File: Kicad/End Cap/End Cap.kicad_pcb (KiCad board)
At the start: 2 copper layers, 45 x 5 mm, 12 parts, among them J1 1.27mm 4 pin header, J2 Keystone 3579, J3 Keystone 3569, J4 Keystone 3579, J5 Keystone 3569, J6 Keystone 3579, J7 Keystone 3569, J8 Keystone 3579, J9 Keystone 3569

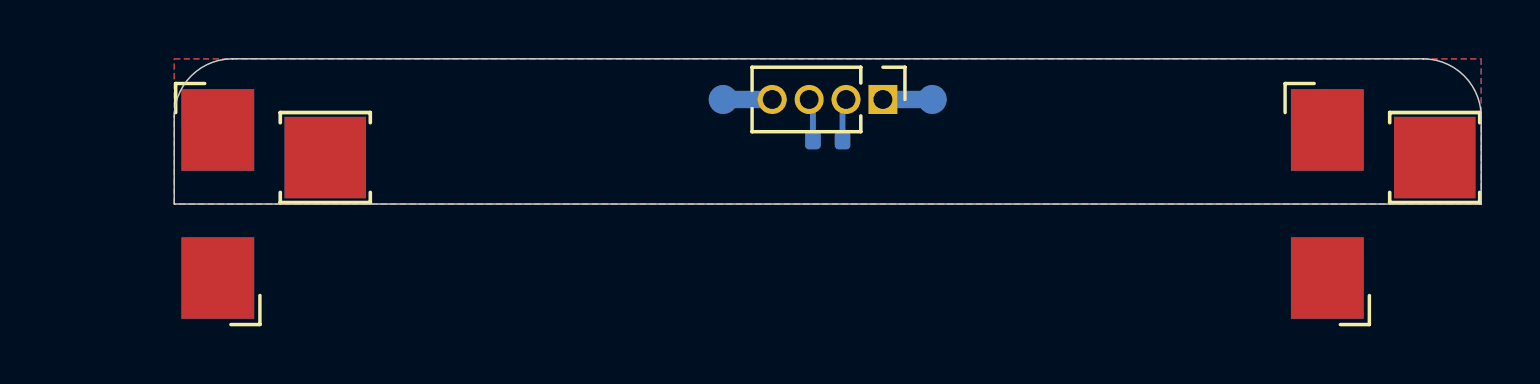
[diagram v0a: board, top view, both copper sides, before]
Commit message: Exported 3D model for End Cap
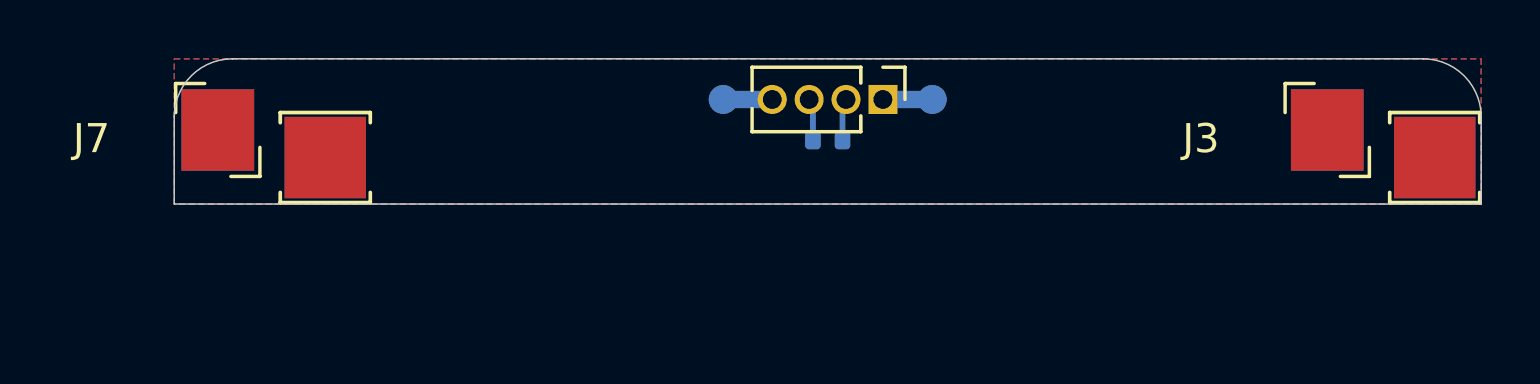
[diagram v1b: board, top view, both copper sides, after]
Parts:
- J3, J5, J7, J9: footprint custom_Connector:Keystone_3569 -> custom_Connector:Keystone_3569_half
- turned J3 to 180 degrees
- turned J5 to 0 degrees
- turned J7 to 180 degrees
- turned J9 to 0 degrees

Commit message: Fixed headers and connectors miss-alignments
Almost everything was misaligned. The holes on the hub to hub headers must be 2.9mm from the edge, the header holes on the motor drivers must be 4.5mm from the edge, and the centers of the power connectors(either gender) must be 2.15mm from the edge
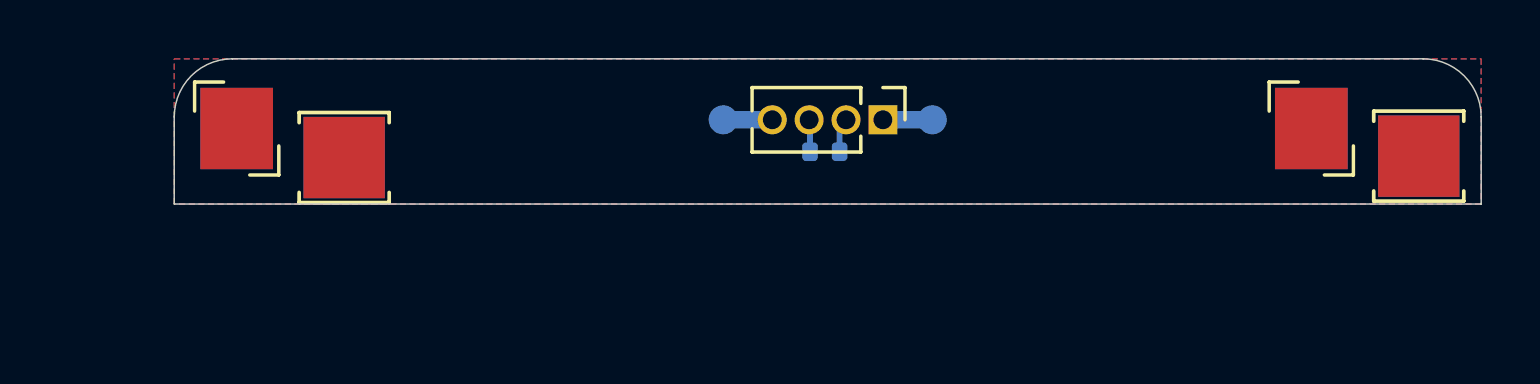
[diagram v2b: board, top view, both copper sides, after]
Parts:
- moved J1 0.70 mm to (144.7, 90.8)
- moved TP3 0.70 mm to (139.2, 90.8)
- moved TP4 0.70 mm to (146.4, 90.8)
- moved J7 0.65 mm to (122.5, 93.7)
- moved J9 0.65 mm to (122.5, 93.7)
- moved J6 0.65 mm to (126.2, 92.1)
- moved J8 0.65 mm to (126.2, 92.1)
- moved J3 0.55 mm to (159.4, 93.7)
- moved J5 0.55 mm to (159.4, 93.7)
- moved J2 0.55 mm to (163.2, 92.0)
- moved J4 0.55 mm to (163.2, 92.0)
- moved R1 0.41 mm to (142.7, 91.9)
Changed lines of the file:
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@@
 	(footprint "Connector_PinHeader_1.27mm:PinHeader_1x04_P1.27mm_Vertical"
 		(layer "F.Cu")
-		(at 144.7 90.1 -90)
+		(at 144.7 90.8 -90)
 		(descr "Through hole straight pin header, 1x04, 1.27mm pitch, single row")
 		(tags "Through hole pin header THT 1x04 1.27mm single row")
@@
 	(footprint "custom_Connector:Keystone_3569_half"
 		(layer "F.Cu")
-		(at 160 93.7 180)
+		(at 159.45 93.65 180)
 		(descr "Fuse Clip 15 A 500V 1 Circuit Blade Surface Mount. Also goes with Keystone 3579 board edge conn")
 		(tags "Fuse")
 		(property "Reference" "J3"
-			(at 4.35 2.25 0)
-			(layer "F.SilkS")
+			(at 0.8 0.4 0)
+			(layer "F.SilkS")
+			(hide yes)
 			(effects
 				(font
@@
 	(footprint "custom_Connector:Keystone_3579"
 		(layer "F.Cu")
-		(at 163.7 92.1)
+		(at 163.15 92.05)
 		(property "Reference" "J2"
 			(at 0.882 -3.3964 0)
@@
 	(footprint "custom_Connector:Keystone_3569_half"
 		(layer "F.Cu")
-		(at 121.8 93.7 180)
+		(at 122.45 93.65 180)
 		(descr "Fuse Clip 15 A 500V 1 Circuit Blade Surface Mount. Also goes with Keystone 3579 board edge conn")
 		(tags "Fuse")
 		(property "Reference" "J7"
-			(at 4.35 2.25 0)
-			(layer "F.SilkS")
+			(at 0.65 0.25 0)
+			(layer "F.SilkS")
+			(hide yes)
 			(effects
 				(font
@@
 	(footprint "custom_Connector:Keystone_3579"
 		(layer "F.Cu")
-		(at 125.5 92.1)
+		(at 126.150001 92.1)
 		(property "Reference" "J6"
 			(at 0.882 -3.3964 0)
@@
 	(footprint "TestPoint:TestPoint_Pad_D1.0mm"
 		(layer "B.Cu")
-		(at 139.2 90.1 180)
+		(at 139.2 90.8 180)
 		(descr "SMD pad as test Point, diameter 1.0mm")
 		(tags "test point SMD pad")
@@
 	(footprint "custom_Connector:Keystone_3569_half"
 		(layer "B.Cu")
-		(at 160 93.7)
+		(at 159.45 93.65)
 		(descr "Fuse Clip 15 A 500V 1 Circuit Blade Surface Mount. Also goes with Keystone 3579 board edge conn")
 		(tags "Fuse")
 		(property "Reference" "J5"
-			(at 4.35 -2.25 0)
-			(layer "B.SilkS")
+			(at -0.3 0.4 0)
+			(layer "B.SilkS")
+			(hide yes)
 			(effects
 				(font
@@
 	(footprint "Resistor_SMD:R_0402_1005Metric"
 		(layer "B.Cu")
-		(at 142.8 91.5)
+		(at 142.7 91.9)
 		(descr "Resistor SMD 0402 (1005 Metric), square (rectangular) end terminal, IPC_7351 nominal, (Body size source: IPC-SM-782 page 72, https://www.pcb-3d.com/wordpress/wp-content/uploads/ipc-sm-782a_amendment_1_and_2.pdf), generated with kicad-footprint-generator")
 		(tags "resistor")
@@
 	(footprint "custom_Connector:Keystone_3569_half"
 		(layer "B.Cu")
-		(at 121.8 93.7)
+		(at 122.45 93.65)
 		(descr "Fuse Clip 15 A 500V 1 Circuit Blade Surface Mount. Also goes with Keystone 3579 board edge conn")
 		(tags "Fuse")
 		(property "Reference" "J9"
-			(at 4.35 -2.25 0)
-			(layer "B.SilkS")
+			(at 0.2 0.05 0)
+			(layer "B.SilkS")
+			(hide yes)
 			(effects
 				(font
@@
 	(footprint "TestPoint:TestPoint_Pad_D1.0mm"
 		(layer "B.Cu")
-		(at 146.4 90.1 180)
+		(at 146.4 90.8 180)
 		(descr "SMD pad as test Point, diameter 1.0mm")
 		(tags "test point SMD pad")
@@
 	(footprint "custom_Connector:Keystone_3579"
 		(layer "B.Cu")
-		(at 163.699999 92.1 180)
+		(at 163.15 92.05 180)
 		(property "Reference" "J4"
 			(at 0.882 3.3964 0)
@@
 	(footprint "custom_Connector:Keystone_3579"
 		(layer "B.Cu")
-		(at 125.499999 92.1 180)
+		(at 126.15 92.1 180)
 		(property "Reference" "J8"
 			(at 0.882 3.3964 0)
@@
 	)
 	(segment
-		(start 139.2 90.1)
-		(end 140.89 90.1)
+		(start 139.2 90.8)
+		(end 140.89 90.8)
 		(width 0.6)
 		(layer "B.Cu")
@@
 	)
 	(segment
-		(start 146.4 90.1)
-		(end 144.7 90.1)
+		(start 146.4 90.8)
+		(end 144.7 90.8)
 		(width 0.6)
 		(layer "B.Cu")
@@
 	)
 	(segment
-		(start 143.31 90.22)
-		(end 143.43 90.1)
+		(start 143.21 91.9)
+		(end 143.21 91.02)
 		(width 0.2)
 		(layer "B.Cu")
@@
 	)
 	(segment
-		(start 143.31 91.5)
-		(end 143.31 90.22)
+		(start 143.21 91.02)
+		(end 143.43 90.8)
 		(width 0.2)
 		(layer "B.Cu")
@@
 	)
 	(segment
-		(start 142.29 91.5)
-		(end 142.29 90.23)
+		(start 142.19 91.9)
+		(end 142.19 90.83)
 		(width 0.2)
 		(layer "B.Cu")
@@
 	)
 	(segment
-		(start 142.29 90.23)
-		(end 142.16 90.1)
+		(start 142.19 90.83)
+		(end 142.16 90.8)
 		(width 0.2)
 		(layer "B.Cu")
